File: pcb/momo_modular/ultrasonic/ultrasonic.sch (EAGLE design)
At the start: 39 parts, among them U1 TDC1000, U2 TDC7200, U3 PIC16LF1847

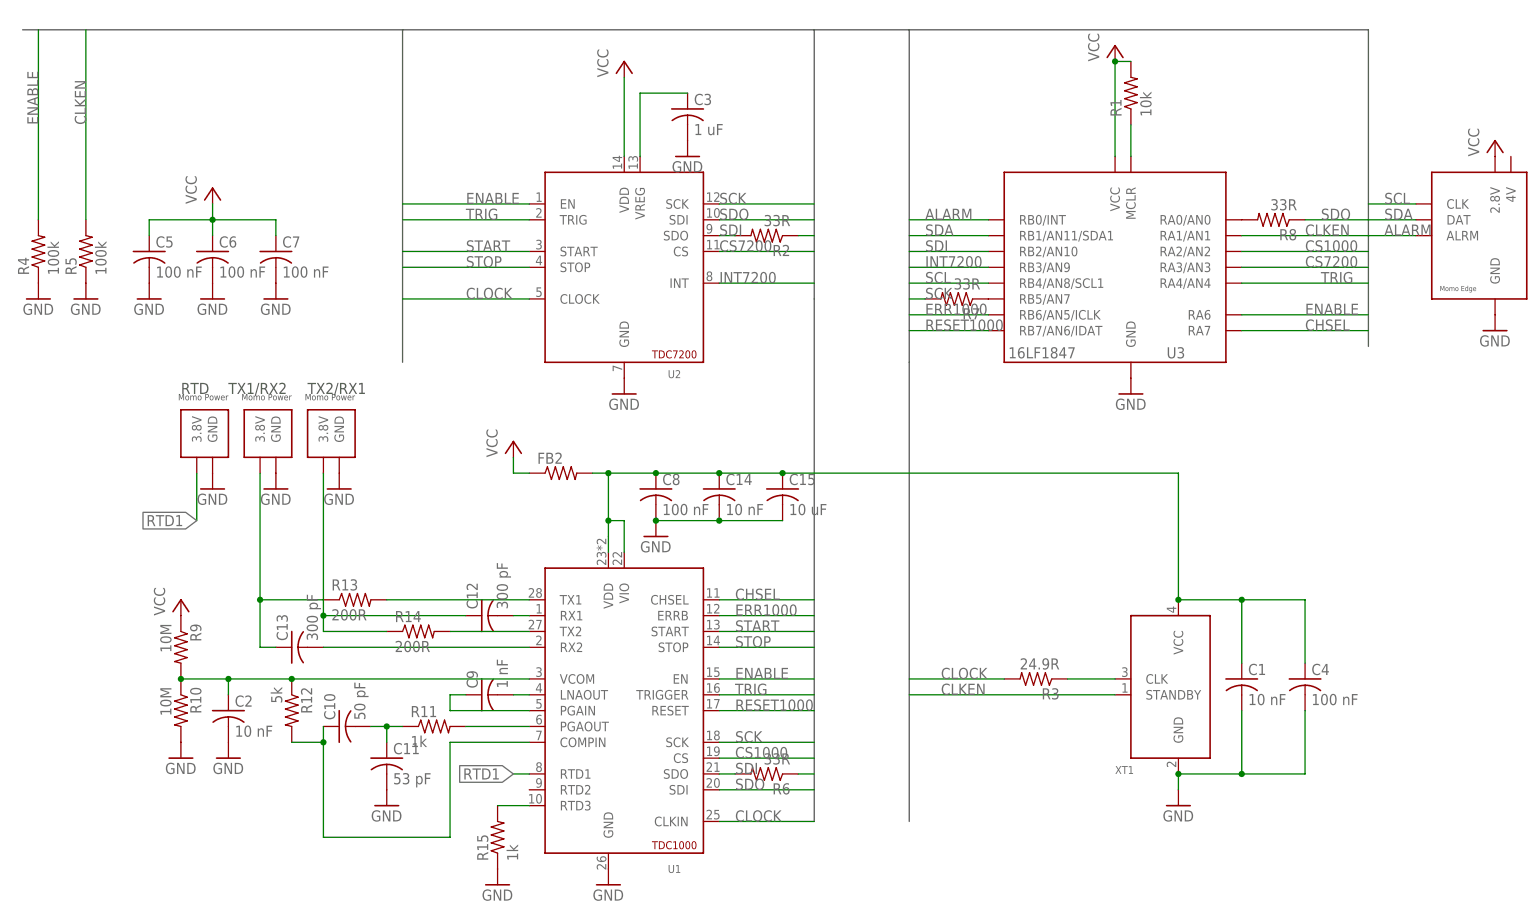
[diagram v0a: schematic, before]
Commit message: Continue layout of ultrasonic board
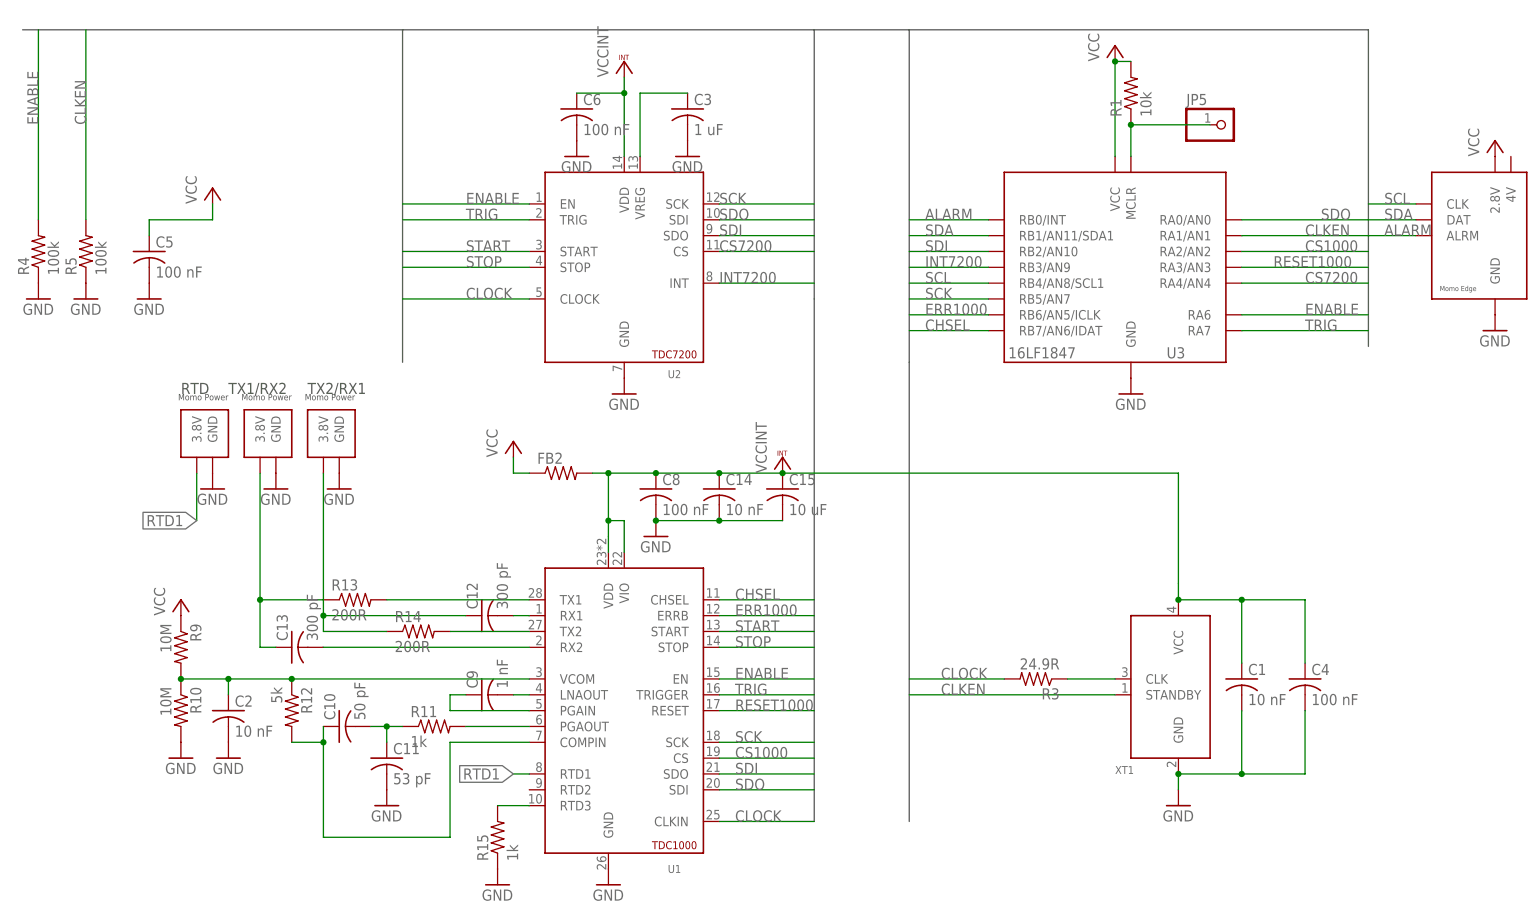
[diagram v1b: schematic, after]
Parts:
- removed C7: 100 nF, rcl:C-USC0402K
- removed R2, R6, R7, R8: 33R, rcl:R-US_R0603
- added JP5: (no value), pinhead:PINHD-1X1
- C3, C5, C6: device rcl:C-USC0402K -> rcl:C-USC0402
- R1, R4, R5: device rcl:R-US_R0603 -> rcl:R-US_R0402
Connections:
- removed net N$1: R2.2, U2.SDO
- removed net N$22: C1.1, C14.1, C15.1, C4.1, C8.1, FB2.2, U1.VDD, U1.VIO, XT1.VCC
- removed net N$5: R6.2, U1.SDO
- removed net N$7: R7.1, U3.RB5/AN7
- removed net N$8: R8.2, U3.RA0/AN0
- new net VCCINT: C1.1, C14.1, C15.1, C4.1, C6.1, C8.1, FB2.2, U1.VDD, U1.VIO, U2.VDD, XT1.VCC
- net CHSEL: now also U3.RB7/AN6/IDAT; no longer U3.RA7
- net CS7200: now also U3.RA4/AN4; no longer U3.RA3/AN3
- net GND: no longer C7.2
- net N$9: now also JP5.1
- net RESET1000: now also U3.RA3/AN3; no longer U3.RB7/AN6/IDAT
- net SCK: now also U3.RB5/AN7; no longer R7.2
- net SDI: now also U1.SDO, U2.SDO; no longer R2.1, R6.1
- net SDO: now also U3.RA0/AN0; no longer R8.1
- net TRIG: now also U3.RA7; no longer U3.RA4/AN4
- net VCC: no longer C6.1, C7.1, U2.VDD
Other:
- moved on the sheet: C6

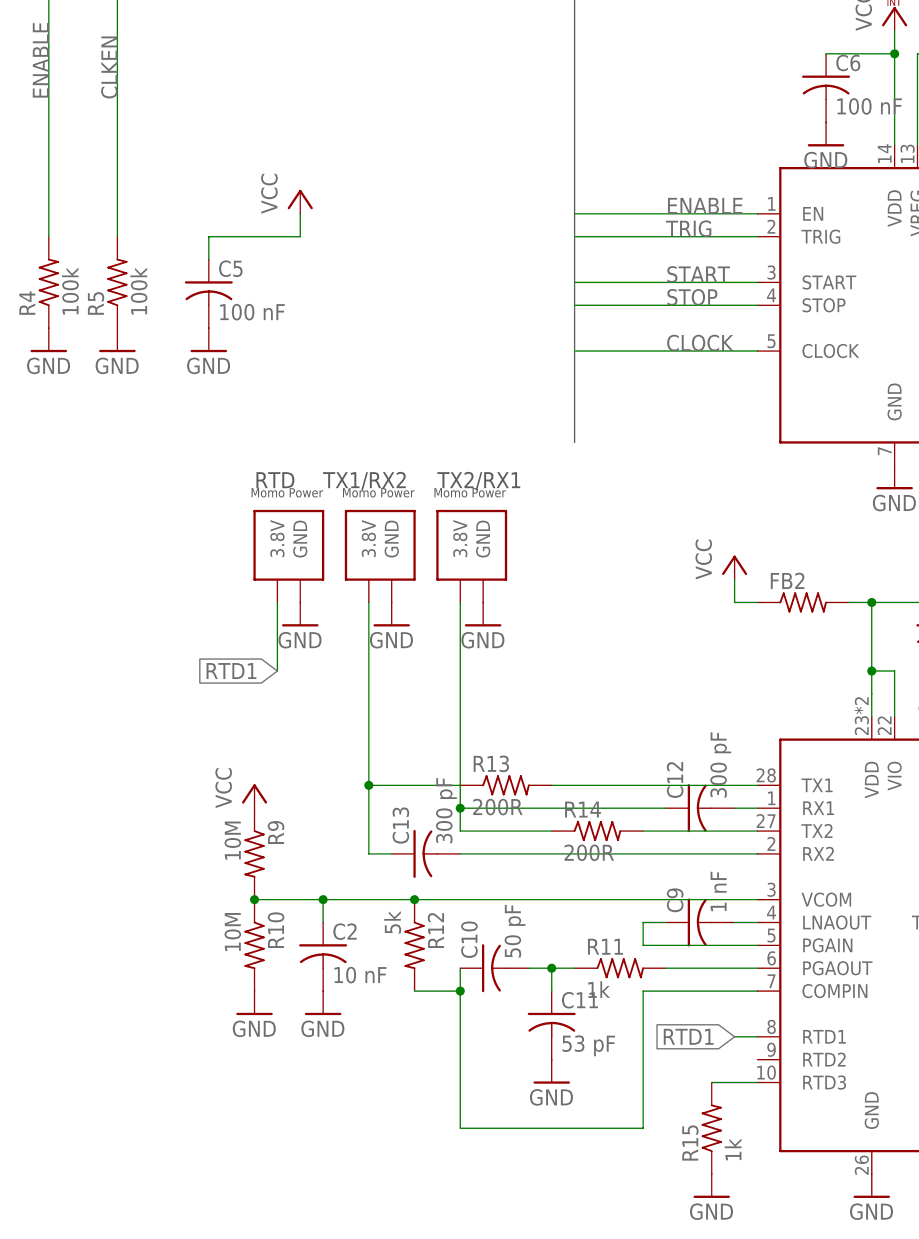
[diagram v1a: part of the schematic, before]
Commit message: Finish layout of ultrasonic board
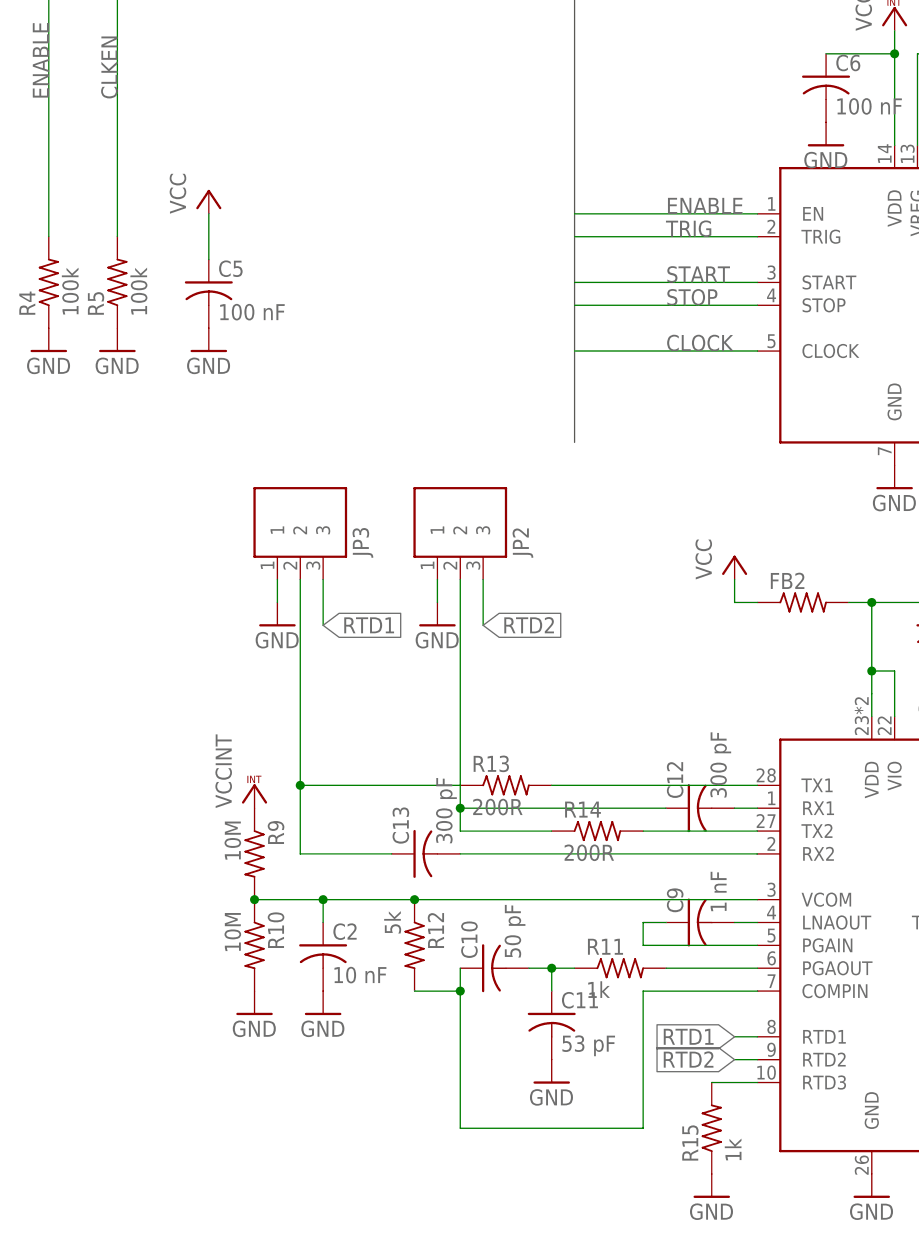
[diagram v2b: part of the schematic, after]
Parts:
- removed JP4: MOMO-PWR-HOUSED, components:MOMO-PWR-HOUSED
- JP2, JP3: value MOMO-PWR-HOUSED -> JST-PH-3PIN; device components:MOMO-PWR-HOUSED -> custom_ics:JST-PH-3PIN
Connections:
- new net RTD2: JP2.3, U1.RTD2
- net GND: now also JP2.1, JP3.1; no longer JP2.GND, JP3.GND, JP4.GND
- net N$15: now also JP3.2; no longer JP3.3.8V
- net N$20: now also JP2.2; no longer JP4.3.8V
- net RTD1: now also JP3.3; no longer JP2.3.8V
- net VCC: no longer R9.1
- net VCCINT: now also R9.1
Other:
- note removed: "RTD"
- note removed: "TX1/RX2"
- note removed: "TX2/RX1"
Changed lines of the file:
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@@
 <part name="R10" library="rcl" deviceset="R-US_" device="R0402" value="10M"/>
 <part name="C2" library="rcl" deviceset="C-US" device="C0402" value="10 nF"/>
-<part name="P+7" library="supply1" deviceset="VCC" device=""/>
 <part name="GND12" library="supply1" deviceset="GND" device=""/>
 <part name="GND13" library="supply1" deviceset="GND" device=""/>
@@
 <part name="C12" library="rcl" deviceset="C-US" device="C0402" value="300 pF"/>
 <part name="C13" library="rcl" deviceset="C-US" device="C0402" value="300 pF"/>
-<part name="JP2" library="components" deviceset="MOMO-PWR-HOUSED" device=""/>
-<part name="JP3" library="components" deviceset="MOMO-PWR-HOUSED" device=""/>
-<part name="JP4" library="components" deviceset="MOMO-PWR-HOUSED" device=""/>
 <part name="GND16" library="supply1" deviceset="GND" device=""/>
 <part name="GND17" library="supply1" deviceset="GND" device=""/>
-<part name="GND18" library="supply1" deviceset="GND" device=""/>
 <part name="R15" library="rcl" deviceset="R-US_" device="R0402" value="1k"/>
 <part name="GND19" library="supply1" deviceset="GND" device=""/>
@@
 <part name="VCC2" library="supply1" deviceset="VCCINT" device=""/>
 <part name="JP5" library="pinhead" deviceset="PINHD-1X1" device=""/>
+<part name="JP2" library="custom_ics" deviceset="JST-PH-3PIN" device=""/>
+<part name="JP3" library="custom_ics" deviceset="JST-PH-3PIN" device=""/>
+<part name="VCC3" library="supply1" deviceset="VCCINT" device=""/>
 </parts>
 <sheets>
 <sheet>
 <plain>
-<text x="-43.18" y="104.14" size="1.778" layer="97">TX1/RX2</text>
-<text x="-30.48" y="104.14" size="1.778" layer="97">TX2/RX1</text>
-<text x="-50.8" y="104.14" size="1.778" layer="97">RTD</text>
 </plain>
 <instances>
@@
 <instance part="GND9" gate="1" x="-55.88" y="119.38"/>
 <instance part="GND10" gate="1" x="12.7" y="142.24"/>
-<instance part="P+5" gate="VCC" x="-45.72" y="137.16"/>
+<instance part="P+5" gate="VCC" x="-55.88" y="137.16"/>
 <instance part="P+6" gate="VCC" x="99.06" y="160.02"/>
 <instance part="R9" gate="G$1" x="-50.8" y="63.5" rot="R270"/>
 <instance part="R10" gate="G$1" x="-50.8" y="53.34" rot="R270"/>
 <instance part="C2" gate="G$1" x="-43.18" y="53.34"/>
-<instance part="P+7" gate="VCC" x="-50.8" y="71.12"/>
 <instance part="GND12" gate="1" x="-50.8" y="45.72"/>
 <instance part="GND13" gate="1" x="-43.18" y="45.72"/>
@@
 <instance part="C12" gate="G$1" x="-2.54" y="68.58" rot="R90"/>
 <instance part="C13" gate="G$1" x="-33.02" y="63.5" rot="R90"/>
-<instance part="JP2" gate="G$1" x="-45.72" y="93.98" rot="R90"/>
-<instance part="JP3" gate="G$1" x="-35.56" y="93.98" rot="R90"/>
-<instance part="JP4" gate="G$1" x="-25.4" y="93.98" rot="R90"/>
-<instance part="GND16" gate="1" x="-25.4" y="88.9"/>
-<instance part="GND17" gate="1" x="-35.56" y="88.9"/>
-<instance part="GND18" gate="1" x="-45.72" y="88.9"/>
+<instance part="GND16" gate="1" x="-30.48" y="88.9"/>
+<instance part="GND17" gate="1" x="-48.26" y="88.9"/>
 <instance part="R15" gate="G$1" x="0" y="33.02" rot="R90"/>
 <instance part="GND19" gate="1" x="0" y="25.4"/>
@@
 <instance part="VCC2" gate="G$1" x="20.32" y="157.48"/>
 <instance part="JP5" gate="G$1" x="116.84" y="147.32"/>
+<instance part="JP2" gate="G$1" x="-27.94" y="99.06" rot="R90"/>
+<instance part="JP3" gate="G$1" x="-45.72" y="99.06" rot="R90"/>
+<instance part="VCC3" gate="G$1" x="-50.8" y="71.12"/>
 </instances>
 <busses>
@@
 </segment>
 <segment>
-<pinref part="JP4" gate="G$1" pin="GND"/>
-<pinref part="GND16" gate="1" pin="GND"/>
-</segment>
-<segment>
-<pinref part="JP3" gate="G$1" pin="GND"/>
-<pinref part="GND17" gate="1" pin="GND"/>
-</segment>
-<segment>
-<pinref part="JP2" gate="G$1" pin="GND"/>
-<pinref part="GND18" gate="1" pin="GND"/>
-</segment>
-<segment>
 <pinref part="R15" gate="G$1" pin="1"/>
 <pinref part="GND19" gate="1" pin="GND"/>
 </segment>
+<segment>
+<pinref part="GND17" gate="1" pin="GND"/>
+<pinref part="JP3" gate="G$1" pin="1"/>
+<wire x1="-48.26" y1="91.44" x2="-48.26" y2="93.98" width="0.1524" layer="91"/>
+</segment>
+<segment>
+<pinref part="GND16" gate="1" pin="GND"/>
+<pinref part="JP2" gate="G$1" pin="1"/>
+<wire x1="-30.48" y1="91.44" x2="-30.48" y2="93.98" width="0.1524" layer="91"/>
+</segment>
 </net>
 <net name="VCC" class="0">
@@
 <segment>
 <pinref part="C5" gate="G$1" pin="1"/>
-<wire x1="-55.88" y1="129.54" x2="-55.88" y2="132.08" width="0.1524" layer="91"/>
-<wire x1="-55.88" y1="132.08" x2="-45.72" y2="132.08" width="0.1524" layer="91"/>
 <pinref part="P+5" gate="VCC" pin="VCC"/>
-<wire x1="-45.72" y1="134.62" x2="-45.72" y2="132.08" width="0.1524" layer="91"/>
+<wire x1="-55.88" y1="134.62" x2="-55.88" y2="129.54" width="0.1524" layer="91"/>
 </segment>
 <segment>
@@
 <pinref part="P+6" gate="VCC" pin="VCC"/>
 <junction x="99.06" y="157.48"/>
-</segment>
-<segment>
-<pinref part="R9" gate="G$1" pin="1"/>
-<pinref part="P+7" gate="VCC" pin="VCC"/>
 </segment>
 <segment>
@@
 <segment>
 <pinref part="R13" gate="G$1" pin="1"/>
-<pinref part="JP3" gate="G$1" pin="3.8V"/>
-<wire x1="-27.94" y1="71.12" x2="-38.1" y2="71.12" width="0.1524" layer="91"/>
-<wire x1="-38.1" y1="71.12" x2="-38.1" y2="91.44" width="0.1524" layer="91"/>
+<wire x1="-27.94" y1="71.12" x2="-45.72" y2="71.12" width="0.1524" layer="91"/>
+<wire x1="-45.72" y1="71.12" x2="-45.72" y2="93.98" width="0.1524" layer="91"/>
 <pinref part="C13" gate="G$1" pin="1"/>
-<wire x1="-35.56" y1="63.5" x2="-38.1" y2="63.5" width="0.1524" layer="91"/>
-<wire x1="-38.1" y1="63.5" x2="-38.1" y2="71.12" width="0.1524" layer="91"/>
-<junction x="-38.1" y="71.12"/>
+<wire x1="-35.56" y1="63.5" x2="-45.72" y2="63.5" width="0.1524" layer="91"/>
+<wire x1="-45.72" y1="63.5" x2="-45.72" y2="71.12" width="0.1524" layer="91"/>
+<junction x="-45.72" y="71.12"/>
+<pinref part="JP3" gate="G$1" pin="2"/>
 </segment>
 </net>
@@
 <segment>
 <pinref part="C12" gate="G$1" pin="1"/>
-<pinref part="JP4" gate="G$1" pin="3.8V"/>
 <wire x1="-5.08" y1="68.58" x2="-27.94" y2="68.58" width="0.1524" layer="91"/>
-<wire x1="-27.94" y1="68.58" x2="-27.94" y2="91.44" width="0.1524" layer="91"/>
+<wire x1="-27.94" y1="68.58" x2="-27.94" y2="93.98" width="0.1524" layer="91"/>
 <pinref part="R14" gate="G$1" pin="1"/>
 <wire x1="-17.78" y1="66.04" x2="-27.94" y2="66.04" width="0.1524" layer="91"/>
 <wire x1="-27.94" y1="66.04" x2="-27.94" y2="68.58" width="0.1524" layer="91"/>
 <junction x="-27.94" y="68.58"/>
+<pinref part="JP2" gate="G$1" pin="2"/>
 </segment>
 </net>
 <net name="RTD1" class="0">
-<segment>
-<pinref part="JP2" gate="G$1" pin="3.8V"/>
-<wire x1="-48.26" y1="91.44" x2="-48.26" y2="83.82" width="0.1524" layer="91"/>
-<label x="-48.26" y="83.82" size="1.778" layer="95" rot="R180" xref="yes"/>
-</segment>
 <segment>
 <pinref part="U1" gate="G$1" pin="RTD1"/>
 <wire x1="5.08" y1="43.18" x2="2.54" y2="43.18" width="0.1524" layer="91"/>
 <label x="2.54" y="43.18" size="1.778" layer="95" rot="R180" xref="yes"/>
+</segment>
+<segment>
+<pinref part="JP3" gate="G$1" pin="3"/>
+<wire x1="-43.18" y1="93.98" x2="-43.18" y2="88.9" width="0.1524" layer="91"/>
+<label x="-43.18" y="88.9" size="1.778" layer="95" xref="yes"/>
 </segment>
 </net>
@@
 <junction x="20.32" y="152.4"/>
 </segment>
-</net>
+<segment>
+<pinref part="R9" gate="G$1" pin="1"/>
+<pinref part="VCC3" gate="G$1" pin="VCCINT"/>
+</segment>
+</net>
+<net name="RTD2" class="0">
+<segment>
+<pinref part="U1" gate="G$1" pin="RTD2"/>
+<wire x1="5.08" y1="40.64" x2="2.54" y2="40.64" width="0.1524" layer="91"/>
+<label x="2.54" y="40.64" size="1.778" layer="95" rot="R180" xref="yes"/>
+</segment>
+<segment>
+<pinref part="JP2" gate="G$1" pin="3"/>
+<wire x1="-25.4" y1="93.98" x2="-25.4" y2="88.9" width="0.1524" layer="91"/>
+<label x="-25.4" y="88.9" size="1.778" layer="95" xref="yes"/>
+</segment>
+</net>
